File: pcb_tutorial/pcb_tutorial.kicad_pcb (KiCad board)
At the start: 2 copper layers, 24 parts, among them SW1 SW_Push, U1 ATmega32U4-A, Y1 16MHz

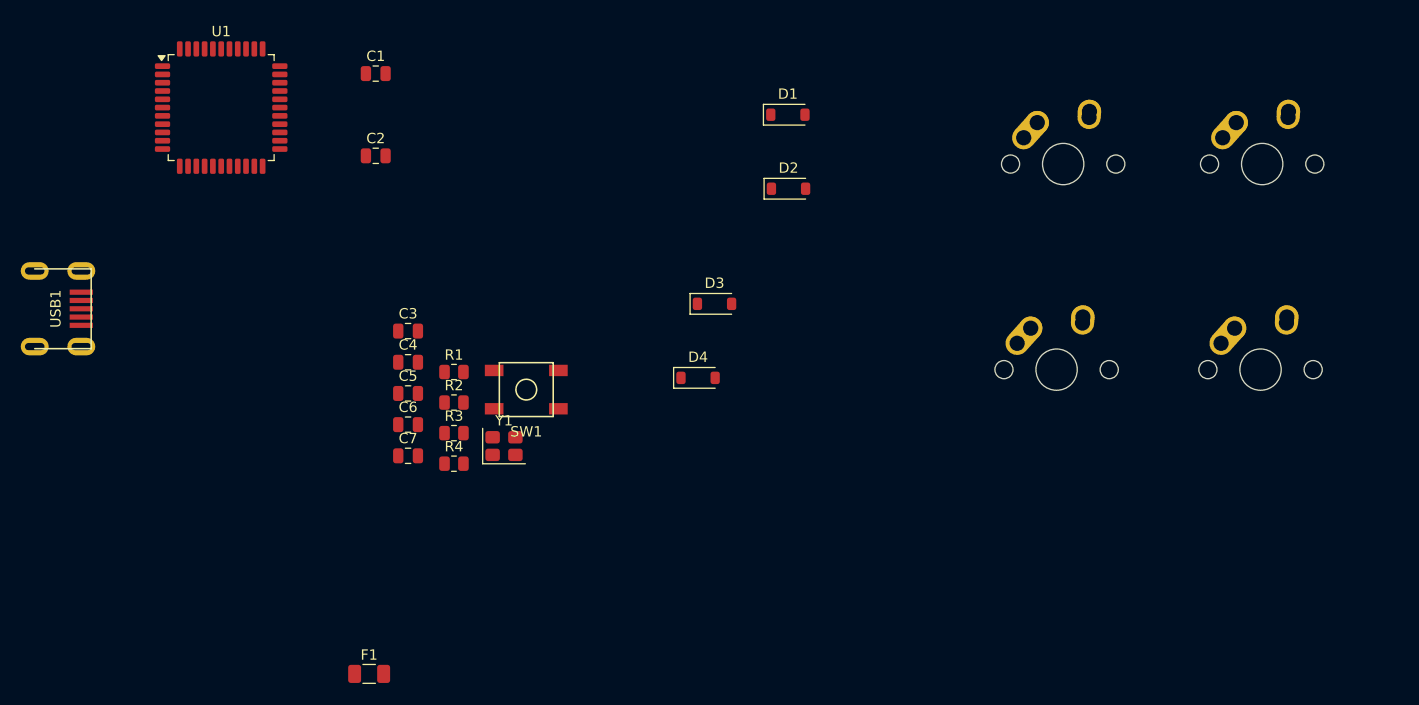
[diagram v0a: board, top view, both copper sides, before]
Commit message: pcb components placed in their places
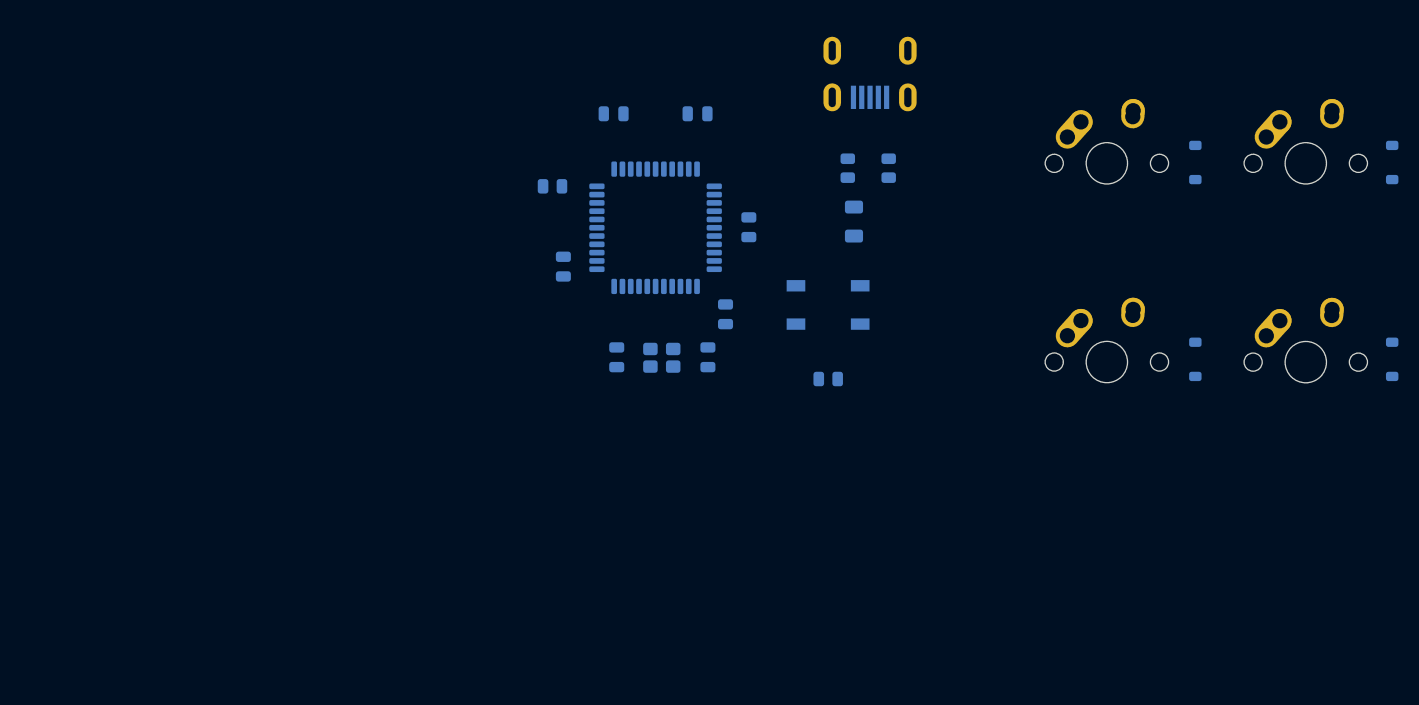
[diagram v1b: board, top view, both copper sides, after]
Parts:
- C1, C2, C3, C4, C5, C6, C7, D1, D2, D3, D4, F1, R1, R2, R3, R4, SW1, U1, USB1, Y1: moved to B.Cu
- moved USB1 84.4 mm to (181.7, 58.9), turned to -90 degrees
- moved D4 67.0 mm to (232.1, 88.7), turned to 90 degrees
- moved F1 64.0 mm to (180.2, 75.4), turned to -90 degrees
- moved D2 58.3 mm to (232.1, 69.7), turned to 90 degrees
- moved R2 47.7 mm to (183.5, 70.2), turned to 90 degrees
- moved D3 46.7 mm to (213.1, 88.7), turned to 90 degrees
- moved R3 45.8 mm to (179.6, 70.2), turned to 90 degrees
- moved U1 43.5 mm to (161.0, 76.0), turned to 180 degrees
- moved C1 42.2 mm to (166.1, 88.5), turned to -90 degrees
- moved C6 41.0 mm to (165.1, 65.0), turned to 180 degrees
- moved C7 39.6 mm to (170.0, 76.0), turned to 90 degrees
- moved D1 39.6 mm to (213.1, 69.7), turned to 90 degrees
- moved R1 36.1 mm to (177.7, 90.6)
- moved C5 31.6 mm to (167.8, 84.3), turned to -90 degrees
- moved C2 30.3 mm to (157.2, 88.5), turned to 90 degrees
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
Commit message: Connecting components
Making the worst designed pcb ever
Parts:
- moved C4 28.0 mm to (180.0, 76.8), turned to 0 degrees
- moved R1 22.0 mm to (156.6, 84.2), turned to -90 degrees
- moved SW1 21.1 mm to (159.1, 93.5)
- moved C3 8.49 mm to (165.4, 63.8)
- moved R4 8.06 mm to (158.1, 68.1), turned to 90 degrees
- moved F1 7.66 mm to (176.8, 68.5), turned to 90 degrees
- moved C5 5.98 mm to (173.7, 83.4)
- moved USB1 5.71 mm to (186.5, 62.0)
- moved C7 5.34 mm to (175.3, 75.4)
- moved C1 5.24 mm to (171.2, 87.3)
- moved C2 5.24 mm to (162.3, 87.3)
- moved C6 5.24 mm to (170.2, 63.8)
- moved U1 5.24 mm to (166.1, 74.8)
- moved Y1 5.24 mm to (166.7, 87.3)
- moved R3 4.62 mm to (184.1, 71.1), turned to -90 degrees
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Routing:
- net GND: track 0.00 -> 135.0 mm
- net +5V: track 0.00 -> 41.6 mm
- net ROW1: track 0.00 -> 19.8 mm
- net ROW0: track 0.00 -> 19.6 mm
- net COL1: track 0.00 -> 19.2 mm
- net COL0: track 0.00 -> 19.2 mm
- net Net-(U1-D+): track 0.00 -> 15.7 mm
- net Net-(U1-D-): track 0.00 -> 12.5 mm
- net Net-(U1-XTAL2): track 0.00 -> 11.6 mm
- net VCC: track 0.00 -> 10.0 mm
- net Net-(U1-XTAL1): track 0.00 -> 9.56 mm
- net Net-(U1-~{RESET}): track 0.00 -> 8.90 mm
- net Net-(D3-A): track 0.00 -> 7.31 mm
- net Net-(D2-A): track 0.00 -> 7.19 mm
- net Net-(D1-A): track 0.00 -> 7.19 mm
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
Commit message: Done
The PCB is completed. And it looks really ugly.
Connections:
- U1 pad 10: unconnected-(U1-PB2-Pad10) -> COL0
- U1 pad 11: unconnected-(U1-PB3-Pad11) -> ROW1
- U1 pad 8: unconnected-(U1-PB0-Pad8) -> ROW0
- U1 pad 9: unconnected-(U1-PB1-Pad9) -> COL1
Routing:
- net COL1: track 19.2 -> 71.2 mm
- net ROW1: track 19.8 -> 66.7 mm
- net ROW0: track 19.6 -> 64.3 mm
- net COL0: track 19.2 -> 51.7 mm
- added copper zone on B.Cu, net GND
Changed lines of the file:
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@@
 	(net 25 "unconnected-(U1-PD5-Pad22)")
 	(net 26 "unconnected-(U1-PD7-Pad27)")
-	(net 27 "unconnected-(U1-PB0-Pad8)")
-	(net 28 "unconnected-(U1-PF4-Pad39)")
-	(net 29 "unconnected-(U1-PC6-Pad31)")
-	(net 30 "unconnected-(U1-PB5-Pad29)")
-	(net 31 "unconnected-(U1-PF5-Pad38)")
-	(net 32 "unconnected-(U1-PD3-Pad21)")
-	(net 33 "unconnected-(U1-PB2-Pad10)")
-	(net 34 "unconnected-(U1-PD4-Pad25)")
-	(net 35 "unconnected-(U1-PB3-Pad11)")
-	(net 36 "unconnected-(U1-PD1-Pad19)")
-	(net 37 "unconnected-(U1-PB4-Pad28)")
-	(net 38 "unconnected-(U1-PF6-Pad37)")
-	(net 39 "unconnected-(U1-AREF-Pad42)")
-	(net 40 "unconnected-(U1-PD0-Pad18)")
-	(net 41 "unconnected-(U1-PF0-Pad41)")
-	(net 42 "unconnected-(U1-PD2-Pad20)")
-	(net 43 "unconnected-(U1-PC7-Pad32)")
-	(net 44 "unconnected-(U1-PB7-Pad12)")
-	(net 45 "unconnected-(U1-PB1-Pad9)")
-	(net 46 "unconnected-(U1-PB6-Pad30)")
-	(net 47 "unconnected-(USB1-SHIELD-Pad6)")
-	(net 48 "unconnected-(USB1-ID-Pad2)")
+	(net 27 "unconnected-(U1-PF4-Pad39)")
+	(net 28 "unconnected-(U1-PC6-Pad31)")
+	(net 29 "unconnected-(U1-PB5-Pad29)")
+	(net 30 "unconnected-(U1-PF5-Pad38)")
+	(net 31 "unconnected-(U1-PD3-Pad21)")
+	(net 32 "unconnected-(U1-PD4-Pad25)")
+	(net 33 "unconnected-(U1-PD1-Pad19)")
+	(net 34 "unconnected-(U1-PB4-Pad28)")
+	(net 35 "unconnected-(U1-PF6-Pad37)")
+	(net 36 "unconnected-(U1-AREF-Pad42)")
+	(net 37 "unconnected-(U1-PD0-Pad18)")
+	(net 38 "unconnected-(U1-PF0-Pad41)")
+	(net 39 "unconnected-(U1-PD2-Pad20)")
+	(net 40 "unconnected-(U1-PC7-Pad32)")
+	(net 41 "unconnected-(U1-PB7-Pad12)")
+	(net 42 "unconnected-(U1-PB6-Pad30)")
+	(net 43 "unconnected-(USB1-SHIELD-Pad6)")
+	(net 44 "unconnected-(USB1-ID-Pad2)")
 	(footprint "MX_Alps_Hybrid:MX-1U-NoLED"
 		(layer "F.Cu")
@@
 			(size 2.25 0.5)
 			(layers "B.Cu" "B.Mask" "B.Paste")
-			(net 48 "unconnected-(USB1-ID-Pad2)")
+			(net 44 "unconnected-(USB1-ID-Pad2)")
 			(pinfunction "ID")
 			(pintype "input")
@@
 			(layers "*.Cu" "*.Mask")
 			(remove_unused_layers no)
-			(net 47 "unconnected-(USB1-SHIELD-Pad6)")
+			(net 43 "unconnected-(USB1-SHIELD-Pad6)")
 			(pinfunction "SHIELD")
 			(pintype "input")
@@
 			(layers "*.Cu" "*.Mask")
 			(remove_unused_layers no)
-			(net 47 "unconnected-(USB1-SHIELD-Pad6)")
+			(net 43 "unconnected-(USB1-SHIELD-Pad6)")
 			(pinfunction "SHIELD")
 			(pintype "input")
@@
 			(layers "*.Cu" "*.Mask")
 			(remove_unused_layers no)
-			(net 47 "unconnected-(USB1-SHIELD-Pad6)")
+			(net 43 "unconnected-(USB1-SHIELD-Pad6)")
 			(pinfunction "SHIELD")
 			(pintype "input")
@@
 			(layers "*.Cu" "*.Mask")
 			(remove_unused_layers no)
-			(net 47 "unconnected-(USB1-SHIELD-Pad6)")
+			(net 43 "unconnected-(USB1-SHIELD-Pad6)")
 			(pinfunction "SHIELD")
 			(pintype "input")
@@
 			(layers "B.Cu" "B.Mask" "B.Paste")
 			(roundrect_rratio 0.25)
-			(net 27 "unconnected-(U1-PB0-Pad8)")
+			(net 7 "ROW0")
 			(pinfunction "PB0")
 			(pintype "bidirectional")
@@
 			(layers "B.Cu" "B.Mask" "B.Paste")
 			(roundrect_rratio 0.25)
-			(net 45 "unconnected-(U1-PB1-Pad9)")
+			(net 14 "COL1")
 			(pinfunction "PB1")
 			(pintype "bidirectional")
@@
 			(layers "B.Cu" "B.Mask" "B.Paste")
 			(roundrect_rratio 0.25)
-			(net 33 "unconnected-(U1-PB2-Pad10)")
+			(net 13 "COL0")
 			(pinfunction "PB2")
 			(pintype "bidirectional")
@@
 			(layers "B.Cu" "B.Mask" "B.Paste")
 			(roundrect_rratio 0.25)
-			(net 35 "unconnected-(U1-PB3-Pad11)")
+			(net 10 "ROW1")
 			(pinfunction "PB3")
 			(pintype "bidirectional")
@@
 			(layers "B.Cu" "B.Mask" "B.Paste")
 			(roundrect_rratio 0.25)
-			(net 44 "unconnected-(U1-PB7-Pad12)")
+			(net 41 "unconnected-(U1-PB7-Pad12)")
 			(pinfunction "PB7")
 			(pintype "bidirectional")
@@
 			(layers "B.Cu" "B.Mask" "B.Paste")
 			(roundrect_rratio 0.25)
-			(net 40 "unconnected-(U1-PD0-Pad18)")
+			(net 37 "unconnected-(U1-PD0-Pad18)")
 			(pinfunction "PD0")
 			(pintype "bidirectional")
@@
 			(layers "B.Cu" "B.Mask" "B.Paste")
 			(roundrect_rratio 0.25)
-			(net 36 "unconnected-(U1-PD1-Pad19)")
+			(net 33 "unconnected-(U1-PD1-Pad19)")
 			(pinfunction "PD1")
 			(pintype "bidirectional")
@@
 			(layers "B.Cu" "B.Mask" "B.Paste")
 			(roundrect_rratio 0.25)
-			(net 42 "unconnected-(U1-PD2-Pad20)")
+			(net 39 "unconnected-(U1-PD2-Pad20)")
 			(pinfunction "PD2")
 			(pintype "bidirectional")
@@
 			(layers "B.Cu" "B.Mask" "B.Paste")
 			(roundrect_rratio 0.25)
-			(net 32 "unconnected-(U1-PD3-Pad21)")
+			(net 31 "unconnected-(U1-PD3-Pad21)")
 			(pinfunction "PD3")
 			(pintype "bidirectional")
@@
 			(layers "B.Cu" "B.Mask" "B.Paste")
 			(roundrect_rratio 0.25)
-			(net 34 "unconnected-(U1-PD4-Pad25)")
+			(net 32 "unconnected-(U1-PD4-Pad25)")
 			(pinfunction "PD4")
 			(pintype "bidirectional")
@@
 			(layers "B.Cu" "B.Mask" "B.Paste")
 			(roundrect_rratio 0.25)
-			(net 37 "unconnected-(U1-PB4-Pad28)")
+			(net 34 "unconnected-(U1-PB4-Pad28)")
 			(pinfunction "PB4")
 			(pintype "bidirectional")
@@
 			(layers "B.Cu" "B.Mask" "B.Paste")
 			(roundrect_rratio 0.25)
-			(net 30 "unconnected-(U1-PB5-Pad29)")
+			(net 29 "unconnected-(U1-PB5-Pad29)")
 			(pinfunction "PB5")
 			(pintype "bidirectional")
@@
 			(layers "B.Cu" "B.Mask" "B.Paste")
 			(roundrect_rratio 0.25)
-			(net 46 "unconnected-(U1-PB6-Pad30)")
+			(net 42 "unconnected-(U1-PB6-Pad30)")
 			(pinfunction "PB6")
 			(pintype "bidirectional")
@@
 			(layers "B.Cu" "B.Mask" "B.Paste")
 			(roundrect_rratio 0.25)
-			(net 29 "unconnected-(U1-PC6-Pad31)")
+			(net 28 "unconnected-(U1-PC6-Pad31)")
 			(pinfunction "PC6")
 			(pintype "bidirectional")
@@
 			(layers "B.Cu" "B.Mask" "B.Paste")
 			(roundrect_rratio 0.25)
-			(net 43 "unconnected-(U1-PC7-Pad32)")
+			(net 40 "unconnected-(U1-PC7-Pad32)")
 			(pinfunction "PC7")
 			(pintype "bidirectional")
@@
 			(layers "B.Cu" "B.Mask" "B.Paste")
 			(roundrect_rratio 0.25)
-			(net 38 "unconnected-(U1-PF6-Pad37)")
+			(net 35 "unconnected-(U1-PF6-Pad37)")
 			(pinfunction "PF6")
 			(pintype "bidirectional")
@@
 			(layers "B.Cu" "B.Mask" "B.Paste")
 			(roundrect_rratio 0.25)
-			(net 31 "unconnected-(U1-PF5-Pad38)")
+			(net 30 "unconnected-(U1-PF5-Pad38)")
 			(pinfunction "PF5")
 			(pintype "bidirectional")
@@
 			(layers "B.Cu" "B.Mask" "B.Paste")
 			(roundrect_rratio 0.25)
-			(net 28 "unconnected-(U1-PF4-Pad39)")
+			(net 27 "unconnected-(U1-PF4-Pad39)")
 			(pinfunction "PF4")
 			(pintype "bidirectional")
@@
 			(layers "B.Cu" "B.Mask" "B.Paste")
 			(roundrect_rratio 0.25)
-			(net 41 "unconnected-(U1-PF0-Pad41)")
+			(net 38 "unconnected-(U1-PF0-Pad41)")
 			(pinfunction "PF0")
 			(pintype "bidirectional")
@@
 			(layers "B.Cu" "B.Mask" "B.Paste")
 			(roundrect_rratio 0.25)
-			(net 39 "unconnected-(U1-AREF-Pad42)")
+			(net 36 "unconnected-(U1-AREF-Pad42)")
 			(pinfunction "AREF")
 			(pintype "passive")
@@
 	)
 	(segment
+		(start 174.193899 77.861)
+		(end 172.732899 76.4)
+		(width 0.2)
+		(layer "B.Cu")
+		(net 7)
+	)
+	(segment
 		(start 213.8749 72.1249)
 		(end 231.3251 72.1249)
@@
 	)
 	(segment
+		(start 172.732899 76.4)
+		(end 171.7625 76.4)
+		(width 0.2)
+		(layer "B.Cu")
+		(net 7)
+	)
+	(segment
+		(start 206.589 77.861)
+		(end 174.193899 77.861)
+		(width 0.2)
+		(layer "B.Cu")
+		(net 7)
+	)
+	(segment
+		(start 213.1 71.35)
+		(end 206.589 77.861)
+		(width 0.2)
+		(layer "B.Cu")
+		(net 7)
+	)
+	(segment
 		(start 231.3251 72.1249)
 		(end 232.1 71.35)
@@
 	)
 	(segment
+		(start 173.171 79.064)
+		(end 172.907 78.8)
+		(width 0.2)
+		(layer "B.Cu")
+		(net 10)
+	)
+	(segment
+		(start 213.1 90.35)
+		(end 212.137 91.313)
+		(width 0.2)
+		(layer "B.Cu")
+		(net 10)
+	)
+	(segment
+		(start 172.907 78.8)
+		(end 171.7625 78.8)
+		(width 0.2)
+		(layer "B.Cu")
+		(net 10)
+	)
+	(segment
+		(start 193.3448 91.313)
+		(end 181.0958 79.064)
+		(width 0.2)
+		(layer "B.Cu")
+		(net 10)
+	)
+	(segment
+		(start 181.0958 79.064)
+		(end 173.171 79.064)
+		(width 0.2)
+		(layer "B.Cu")
+		(net 10)
+	)
+	(segment
+		(start 212.137 91.313)
+		(end 193.3448 91.313)
+		(width 0.2)
+		(layer "B.Cu")
+		(net 10)
+	)
+	(segment
 		(start 214.0649 91.3149)
 		(end 231.1351 91.3149)
@@
 	)
 	(segment
+		(start 173.198699 78)
+		(end 171.7625 78)
+		(width 0.2)
+		(layer "B.Cu")
+		(net 13)
+	)
+	(segment
+		(start 192.993 78.663)
+		(end 173.861699 78.663)
+		(width 0.2)
+		(layer "B.Cu")
+		(net 13)
+	)
+	(segment
+		(start 200.75 86.42)
+		(end 192.993 78.663)
+		(width 0.2)
+		(layer "B.Cu")
+		(net 13)
+	)
+	(segment
+		(start 173.861699 78.663)
+		(end 173.198699 78)
+		(width 0.2)
+		(layer "B.Cu")
+		(net 13)
+	)
+	(segment
 		(start 219.95 67.24)
 		(end 219.95 86.43)
@@
 	)
 	(segment
+		(start 172.965799 77.2)
+		(end 171.7625 77.2)
+		(width 0.2)
+		(layer "B.Cu")
+		(net 14)
+	)
+	(segment
+		(start 174.027799 78.262)
+		(end 172.965799 77.2)
+		(width 0.2)
+		(layer "B.Cu")
+		(net 14)
+	)
+	(segment
+		(start 211.782 78.262)
+		(end 174.027799 78.262)
+		(width 0.2)
+		(layer "B.Cu")
+		(net 14)
+	)
+	(segment
+		(start 219.95 86.43)
+		(end 211.782 78.262)
+		(width 0.2)
+		(layer "B.Cu")
+		(net 14)
+	)
+	(segment
 		(start 156.6418 85.4456)
 		(end 162.231 91.0348)
@@
 		(net 20)
 	)
+	(zone
+		(net 2)
+		(net_name "GND")
+		(layer "B.Cu")
+		(hatch edge 0.5)
+		(connect_pads
+			(clearance 0.5)
+		)
+		(min_thickness 0.25)
+		(filled_areas_thickness no)
+		(fill yes
+			(thermal_gap 0.5)
+			(thermal_bridge_width 0.5)
+		)
+		(polygon
+			(pts
+				(xy 153.416 60.198) (xy 194.9704 60.2742) (xy 194.9958 98.4504) (xy 153.67 98.552)
+			)
+		)
+	)
 	(embedded_fonts no)
